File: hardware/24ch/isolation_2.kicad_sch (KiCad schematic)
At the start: 21 parts, among them J401 ENGINE REF FEED/SENSE, Q401 2N7002, Q402 MMBT3906, U408 TLV7031DBVR, U409 TL431

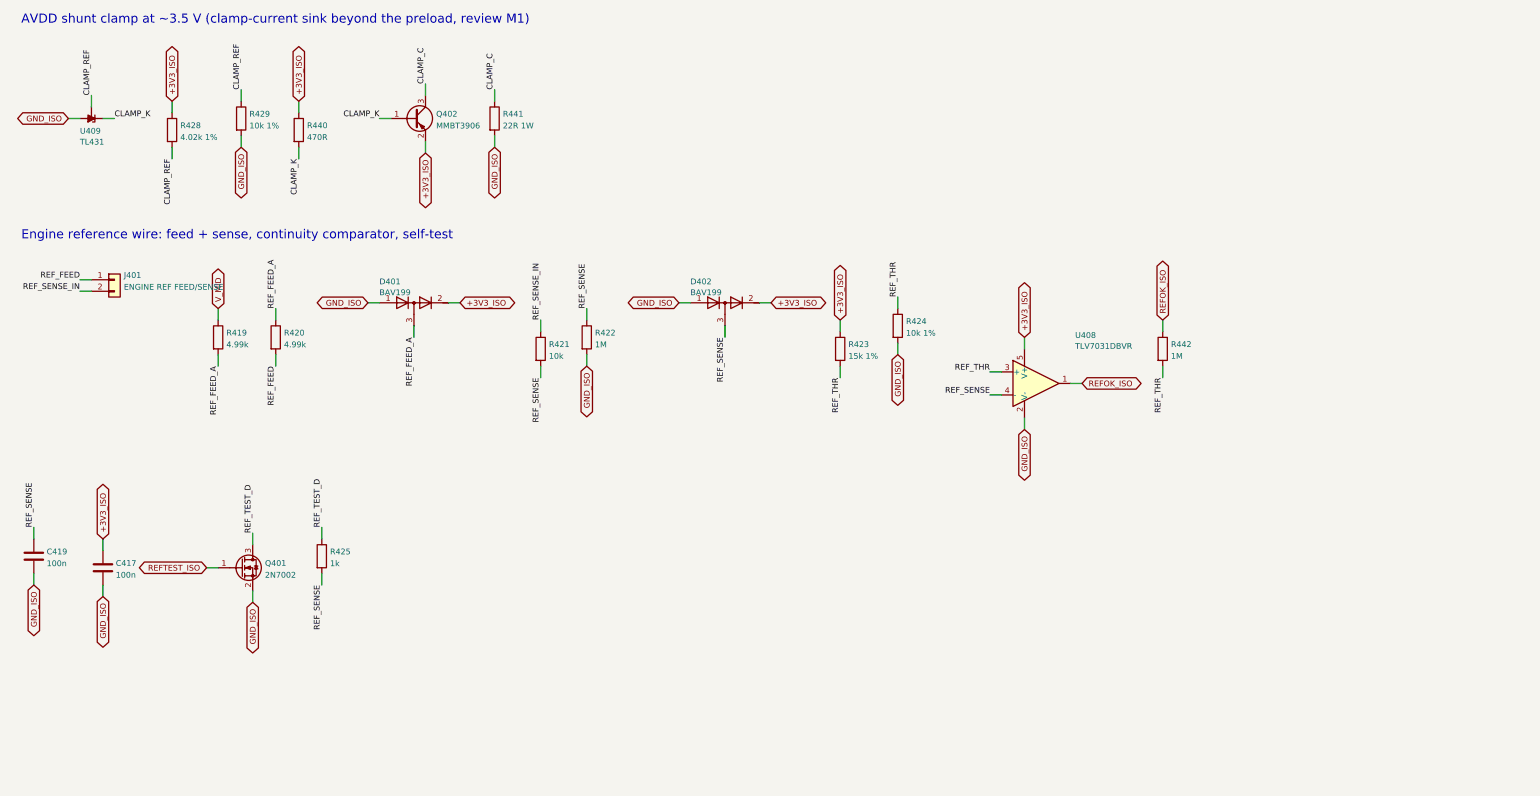
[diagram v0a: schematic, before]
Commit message: 24ch REV A4 (WIP): gated TMP126 SIO driver, PD5 = SIO_WR_N, ESC via diodes
- PD5 (was BTN_ESC) drives SIO_WR_N through spare U405 channel C to U411
  74LVC1G125 (OE); DIN -> U411 -> R446 220R -> DOUT_ISO; R445 10k, R447 100k,
  C421 100n, R439 10k pull-up. R443 22k removed (R446 reuses its footprint).
  Same circuit as hardware/family (fixes the TMP126 SIO edge, 1.2-1.6 us vs 100 ns).
- ESC button kept: D501/D502 1N4148W pull BTN_UP and BTN_DOWN together;
  firmware reads UP+DOWN as ESC.
- Board edited incrementally (delta.py, capnear.py, maze.py with In2 for
  SIO_DRV / SIO_WR_N_ISO); dead DIN branch to the old R443 pad removed.
- Gates: build.py ERC 0 errors 0 warnings, netlist 0 mismatches;
  finish.py DRC (errors, refilled) 0 violations, 0 unconnected; pincaps 0 over
  (U411 added). Silk, full DRC, fab release still to do.
- Title/release names REV A4.

Co-Authored-By: Claude Opus 5.5 <noreply@anthropic.com>
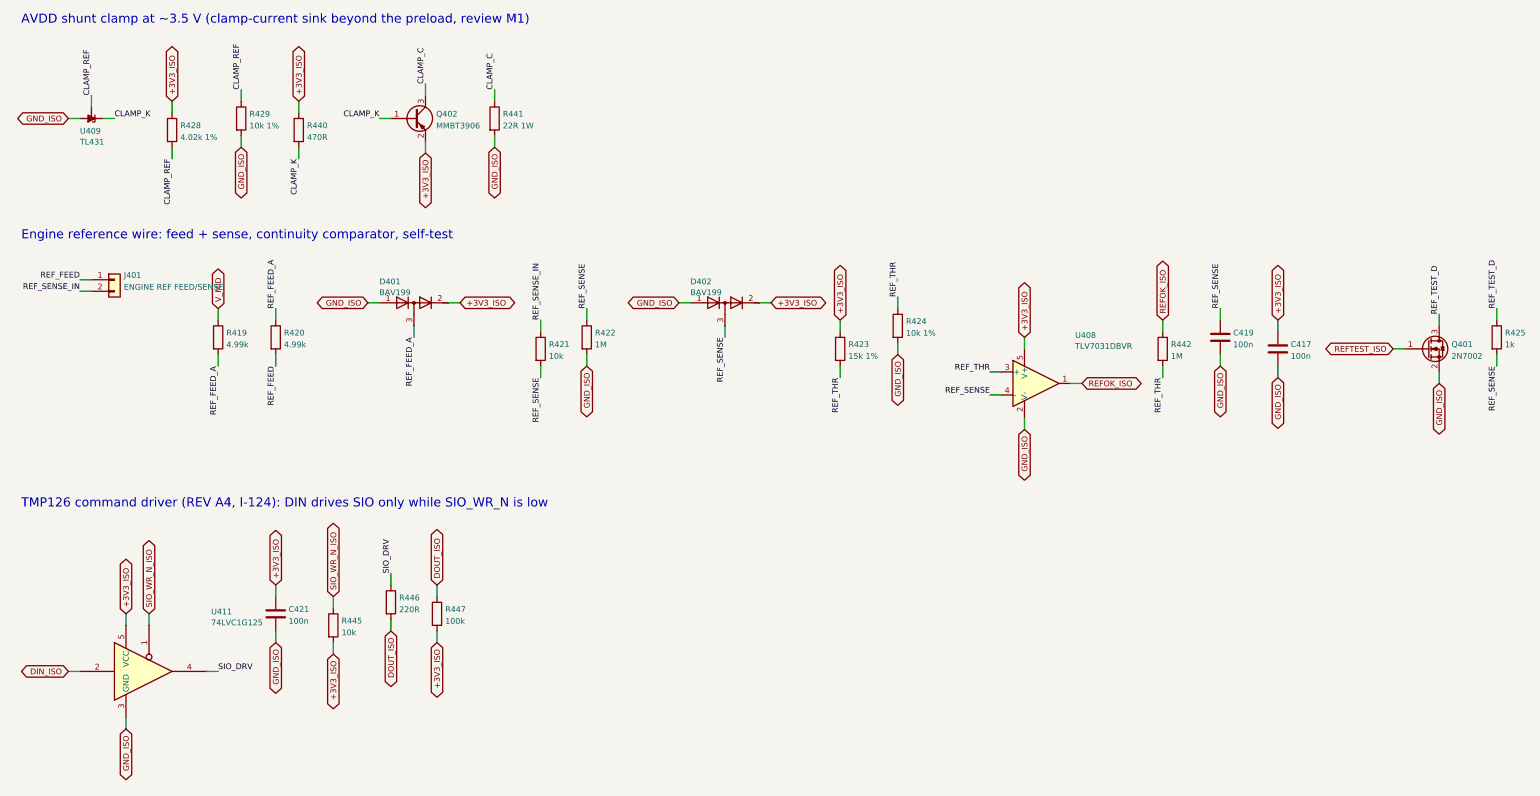
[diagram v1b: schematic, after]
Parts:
- added C421: 100n, Capacitor_SMD:C_0805_2012Metric, symbol Device:C
- added R445: 10k, Resistor_SMD:R_0805_2012Metric, symbol Device:R
- added R446: 220R, Resistor_SMD:R_0805_2012Metric, symbol Device:R
- added R447: 100k, Resistor_SMD:R_0805_2012Metric, symbol Device:R
- added U411: 74LVC1G125, Package_TO_SOT_SMD:SOT-23-5, symbol 74xGxx:74LVC1G125
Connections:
- net +3V3_ISO: now also C421.1, R445.2, R447.2, U411.5 (VCC)
- net GND_ISO: now also C421.2, U411.3 (GND)
- new net DIN_ISO: U411.2
- new net DOUT_ISO: R446.2, R447.1
- new net SIO_DRV: R446.1, U411.4
- new net SIO_WR_N_ISO: R445.1, U411.1
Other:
- note added: "TMP126 command driver (REV A4, I-124): DIN drives SIO only while SIO_WR_N is low"
- moved on the sheet: C417, C419, Q401, R425
